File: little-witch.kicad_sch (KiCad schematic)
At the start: 30 parts, among them J1 GCT-USB4105, J3 Conn_ARM_SWD_TagConnect_TC203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, J4 GCT-USB4105, J5 Conn_02x20_Odd_Even, J6 BOOT0_SEL, SW1 SW_Push, U1 CH32V307RCT6, Y1 SIT8008BI-73-33N-25.000000

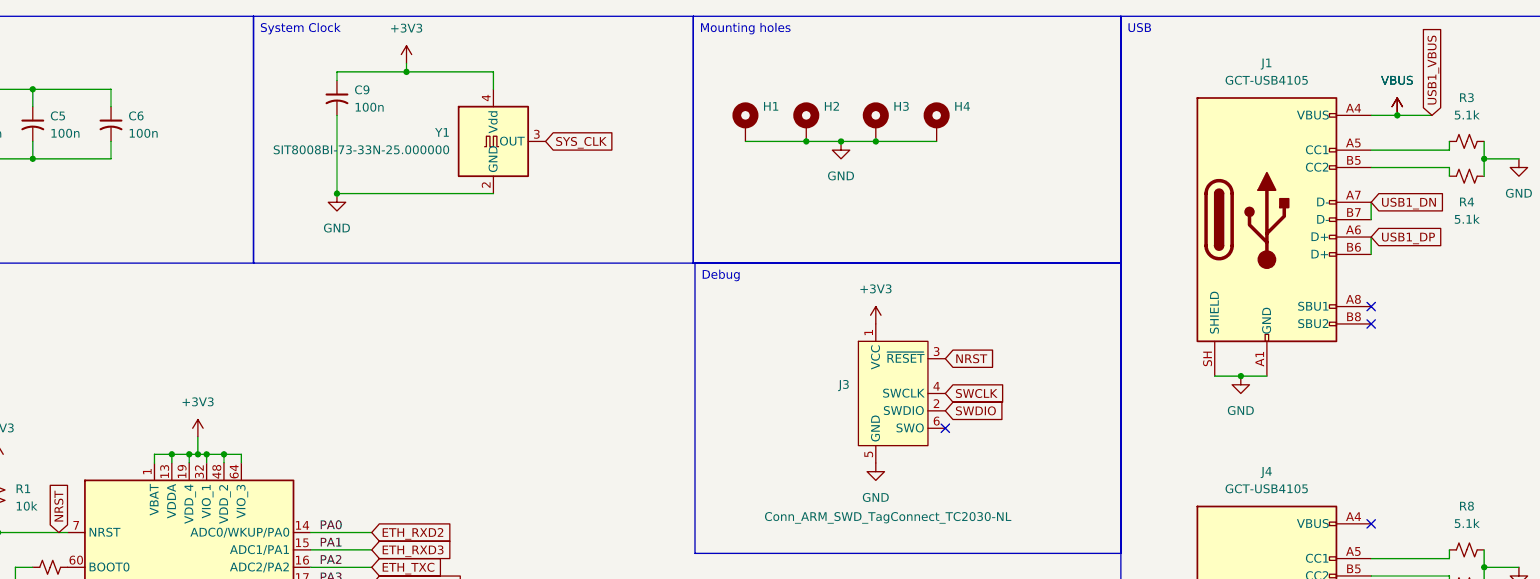
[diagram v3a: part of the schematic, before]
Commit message: Base ethernet signals routed
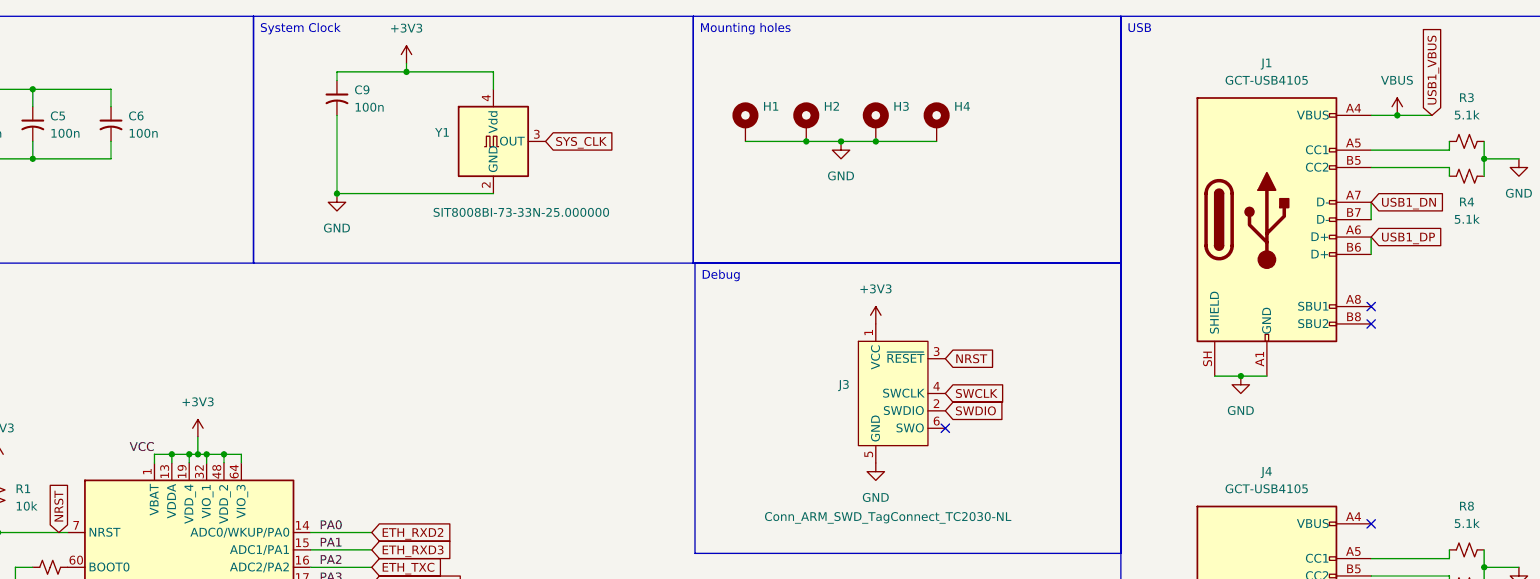
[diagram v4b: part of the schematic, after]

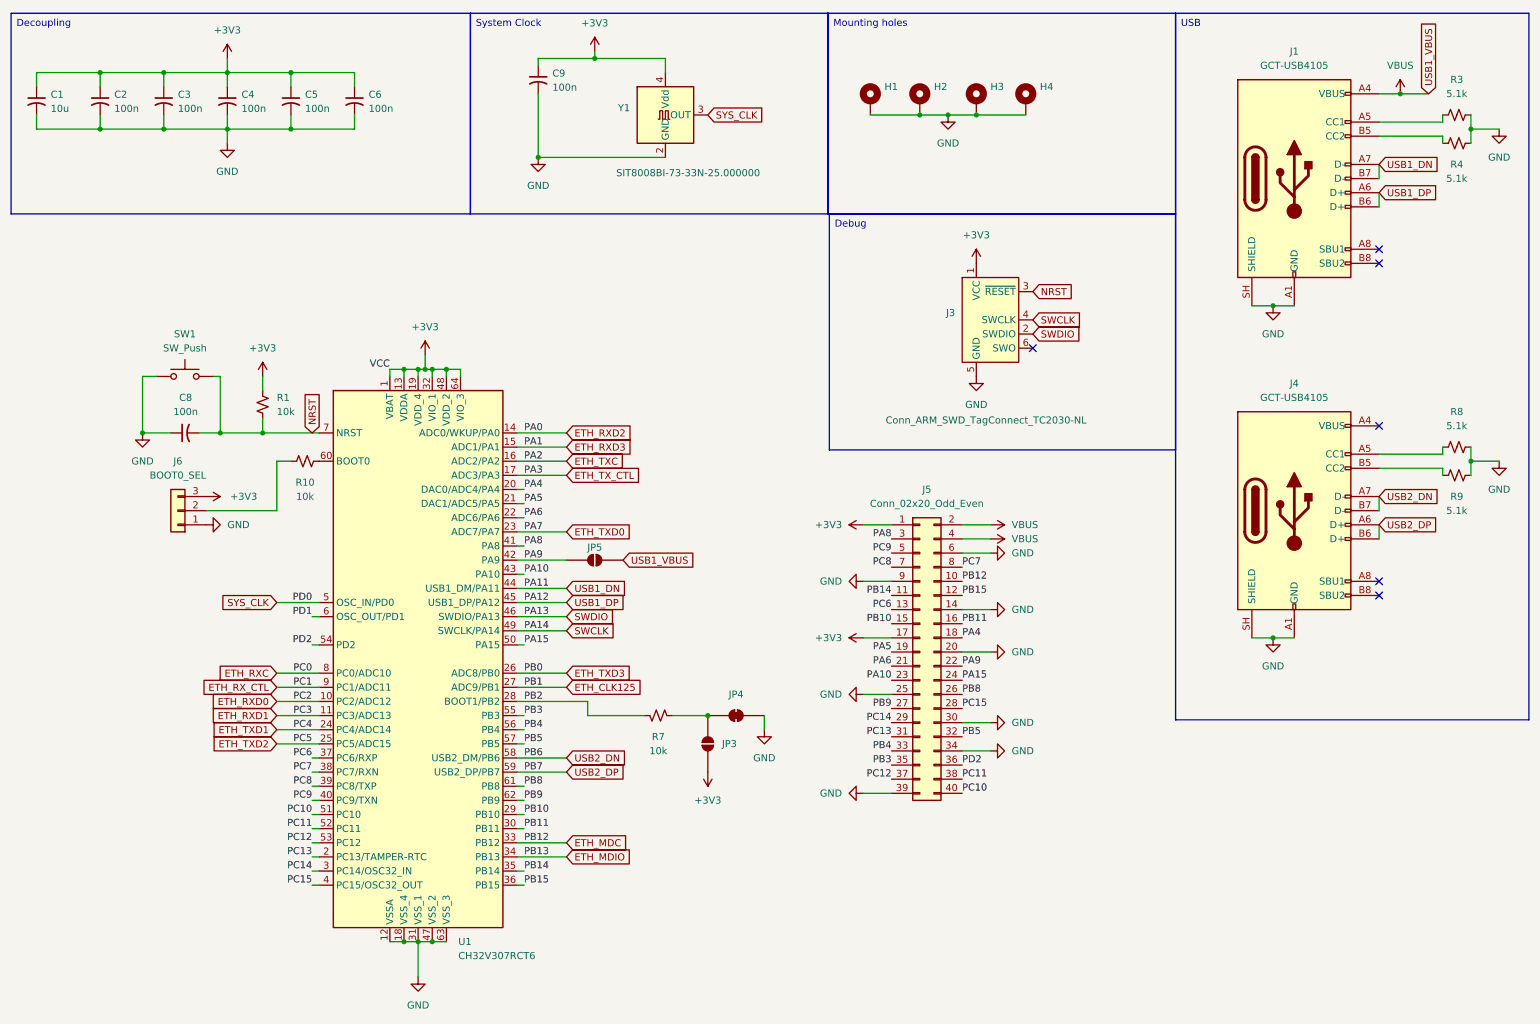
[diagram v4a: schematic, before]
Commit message: Some GPIO and power routing
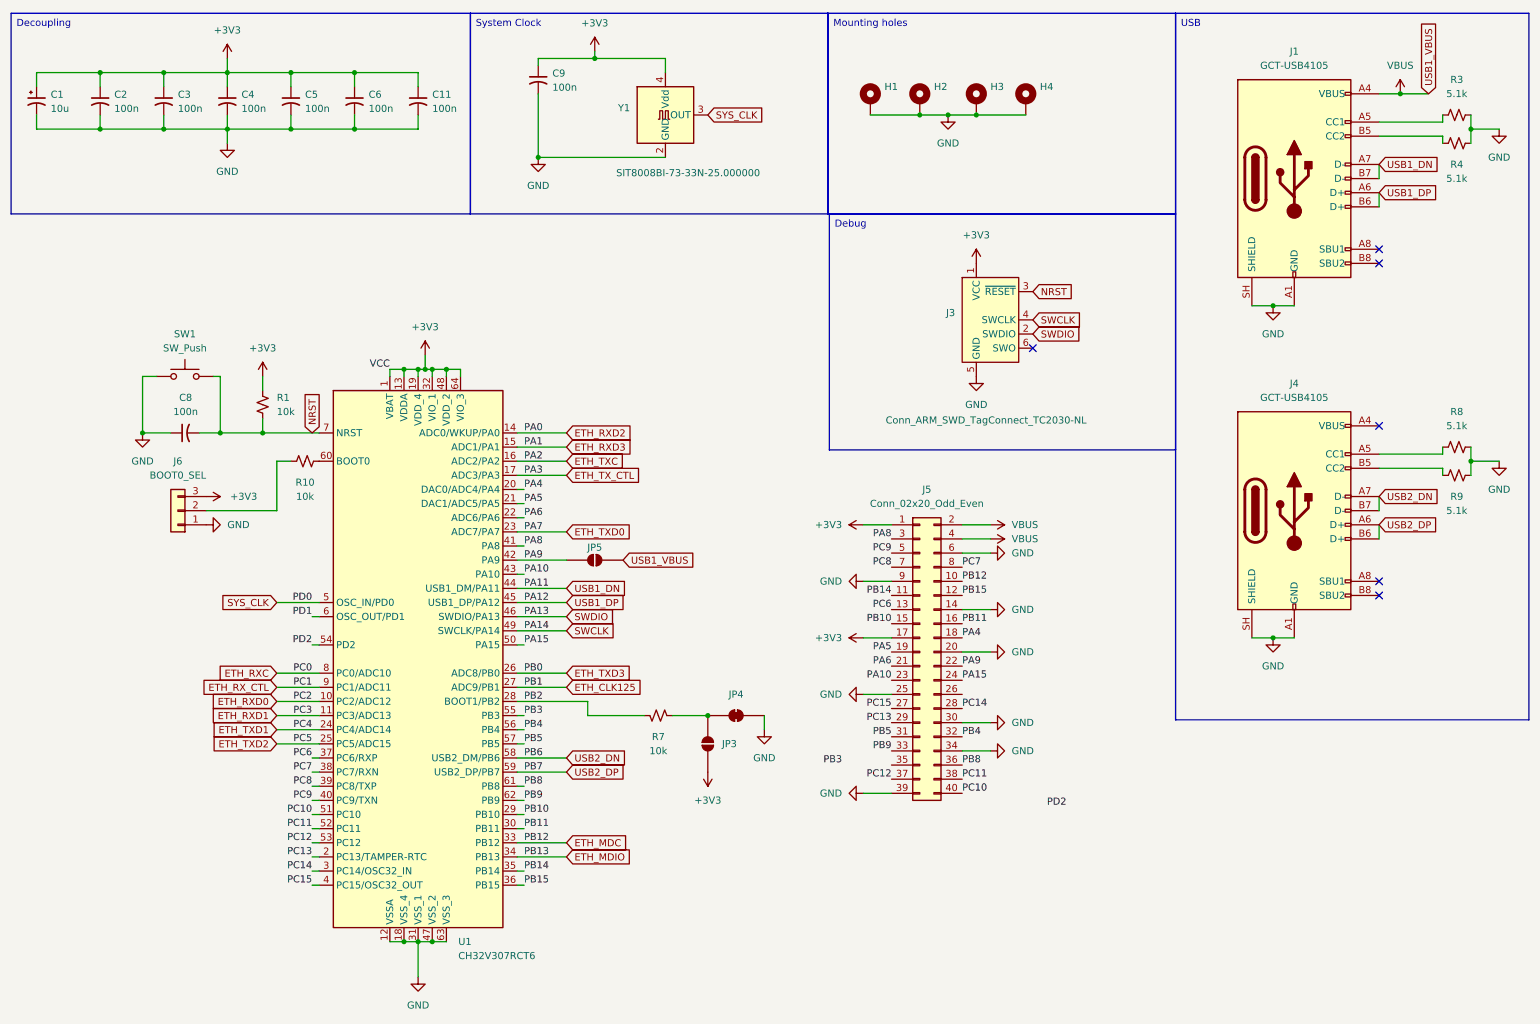
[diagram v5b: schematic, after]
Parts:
- added C11: 100n, Capacitor_SMD:C_0402_1005Metric, symbol Device:C_Small_US
- C1: footprint Capacitor_SMD:C_0402_1005Metric -> Capacitor_Tantalum_SMD:CP_EIA-2012-12_Kemet-R; symbol Device:C_Small_US -> Device:C_Polarized_Small_US
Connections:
- net +3V3: now also C11.1
- net GND: now also C11.2
- net PB3: no longer J5.35 (Pin_35)
- net PB4: now also J5.32 (Pin_32); no longer J5.33 (Pin_33)
- net PB5: now also J5.31 (Pin_31); no longer J5.32 (Pin_32)
- net PB8: now also J5.36 (Pin_36); no longer J5.26 (Pin_26)
- net PB9: now also J5.33 (Pin_33); no longer J5.27 (Pin_27)
- net PC13: now also J5.29 (Pin_29); no longer J5.31 (Pin_31)
- net PC14: now also J5.28 (Pin_28); no longer J5.29 (Pin_29)
- net PC15: now also J5.27 (Pin_27); no longer J5.28 (Pin_28)
- net PD2: no longer J5.36 (Pin_36)
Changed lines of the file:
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@@
 	)
 	(junction
+		(at 73.66 22.86)
+		(diameter 0)
+		(color 0 0 0 0)
+	)
+	(junction
 		(at 39.37 33.02)
 		(diameter 0)
@@
 	)
 	(junction
+		(at 73.66 33.02)
+		(diameter 0)
+		(color 0 0 0 0)
+	)
+	(junction
 		(at 87.63 76.2)
 		(diameter 0)
@@
 	(wire
 		(pts
+			(xy 85.09 33.02) (xy 85.09 30.48)
+		)
+		(stroke
+			(width 0)
+			(type default)
+		)
+	)
+	(wire
+		(pts
 			(xy 35.56 77.47) (xy 38.1 77.47)
 		)
@@
 	(wire
 		(pts
+			(xy 85.09 22.86) (xy 85.09 25.4)
+		)
+		(stroke
+			(width 0)
+			(type default)
+		)
+	)
+	(wire
+		(pts
 			(xy 87.63 76.2) (xy 90.17 76.2)
 		)
@@
 	(wire
 		(pts
+			(xy 73.66 33.02) (xy 85.09 33.02)
+		)
+		(stroke
+			(width 0)
+			(type default)
+		)
+	)
+	(wire
+		(pts
 			(xy 86.36 76.2) (xy 87.63 76.2)
 		)
@@
 	(wire
 		(pts
+			(xy 73.66 22.86) (xy 85.09 22.86)
+		)
+		(stroke
+			(width 0)
+			(type default)
+		)
+	)
+	(wire
+		(pts
 			(xy 116.84 20.32) (xy 129.54 20.32)
 		)
@@
 		)
 	)
-	(label "PC13"
-		(at 170.18 142.24 180)
-		(effects
-			(font
-				(size 1.27 1.27)
-			)
-			(justify right bottom)
-		)
-	)
 	(label "PC12"
 		(at 170.18 149.86 180)
@@
 		)
 	)
-	(label "PC14"
-		(at 170.18 139.7 180)
-		(effects
-			(font
-				(size 1.27 1.27)
-			)
-			(justify right bottom)
-		)
-	)
-	(label "PC15"
-		(at 182.88 137.16 0)
-		(effects
-			(font
-				(size 1.27 1.27)
-			)
-			(justify left bottom)
-		)
-	)
 	(label "PA13"
 		(at 104.14 120.65 0)
@@
 		)
 	)
-	(label "PB4"
-		(at 170.18 144.78 180)
-		(effects
-			(font
-				(size 1.27 1.27)
-			)
-			(justify right bottom)
-		)
-	)
 	(label "PB13"
 		(at 104.14 163.83 0)
@@
 		)
 	)
-	(label "PB5"
-		(at 182.88 142.24 0)
-		(effects
-			(font
-				(size 1.27 1.27)
-			)
-			(justify left bottom)
-		)
-	)
 	(label "PC6"
 		(at 66.04 146.05 180)
@@
 		)
 	)
+	(label "PC13"
+		(at 170.18 139.7 180)
+		(effects
+			(font
+				(size 1.27 1.27)
+			)
+			(justify right bottom)
+		)
+	)
 	(label "PB10"
 		(at 104.14 156.21 0)
@@
 		)
 	)
-	(label "PB8"
-		(at 182.88 134.62 0)
-		(effects
-			(font
-				(size 1.27 1.27)
-			)
-			(justify left bottom)
-		)
-	)
 	(label "PB3"
 		(at 104.14 138.43 0)
@@
 		)
 	)
+	(label "PB3"
+		(at 161.29 147.32 180)
+		(effects
+			(font
+				(size 1.27 1.27)
+			)
+			(justify right bottom)
+		)
+	)
 	(label "PC0"
 		(at 66.04 130.81 180)
@@
 		)
 	)
+	(label "PB5"
+		(at 170.18 142.24 180)
+		(effects
+			(font
+				(size 1.27 1.27)
+			)
+			(justify right bottom)
+		)
+	)
+	(label "PC15"
+		(at 170.18 137.16 180)
+		(effects
+			(font
+				(size 1.27 1.27)
+			)
+			(justify right bottom)
+		)
+	)
 	(label "PA0"
 		(at 104.14 87.63 0)
@@
 	)
 	(label "PB9"
-		(at 170.18 137.16 180)
+		(at 104.14 153.67 0)
 		(effects
 			(font
 				(size 1.27 1.27)
 			)
-			(justify right bottom)
+			(justify left bottom)
 		)
 	)
-	(label "PB9"
-		(at 104.14 153.67 0)
+	(label "PD2"
+		(at 198.12 154.94 0)
 		(effects
 			(font
@@
 		)
 	)
-	(label "PD2"
+	(label "PB8"
 		(at 182.88 147.32 0)
 		(effects
@@
 		)
 	)
+	(label "PB9"
+		(at 170.18 144.78 180)
+		(effects
+			(font
+				(size 1.27 1.27)
+			)
+			(justify right bottom)
+		)
+	)
 	(label "PA4"
 		(at 182.88 124.46 0)
@@
 		)
 	)
-	(label "PC13"
-		(at 66.04 163.83 180)
+	(label "PB4"
+		(at 182.88 142.24 0)
 		(effects
 			(font
 				(size 1.27 1.27)
 			)
-			(justify right bottom)
+			(justify left bottom)
 		)
 	)
-	(label "PB6"
-		(at 104.14 146.05 0)
+	(label "PC14"
+		(at 182.88 137.16 0)
 		(effects
 			(font
@@
 		)
 	)
-	(label "PB3"
-		(at 170.18 147.32 180)
+	(label "PC13"
+		(at 66.04 163.83 180)
 		(effects
 			(font
@@
 		)
 	)
+	(label "PB6"
+		(at 104.14 146.05 0)
+		(effects
+			(font
+				(size 1.27 1.27)
+			)
+			(justify left bottom)
+		)
+	)
 	(label "PC8"
 		(at 170.18 111.76 180)
@@
 	)
 	(symbol
-		(lib_id "Device:C_Small_US")
+		(lib_id "Device:C_Polarized_Small_US")
 		(at 16.51 27.94 0)
 		(unit 1)
@@
 			)
 		)
-		(property "Footprint" "Capacitor_SMD:C_0402_1005Metric"
+		(property "Footprint" "Capacitor_Tantalum_SMD:CP_EIA-2012-12_Kemet-R"
 			(at 16.51 27.94 0)
 			(hide yes)
@@
 			)
 		)
-		(property "Description" "capacitor, small US symbol"
+		(property "Description" "Polarized capacitor, small US symbol"
 			(at 16.51 27.94 0)
 			(hide yes)
@@
 					(unit 1)
 				)
+			)
+		)
+	)
+	(symbol
+		(lib_id "Device:C_Small_US")
+		(at 85.09 27.94 0)
+		(unit 1)
+		(body_style 1)
+		(exclude_from_sim no)
+		(in_bom yes)
+		(on_board yes)
+		(in_pos_files yes)
+		(dnp no)
+		(property "Reference" "C11"
+			(at 87.63 26.7969 0)
+			(show_name no)
+			(do_not_autoplace no)
+			(effects
+				(font
+					(size 1.27 1.27)
+				)
+				(justify left)
+			)
+		)
+		(property "Value" "100n"
+			(at 87.63 29.3369 0)
+			(show_name no)
+			(do_not_autoplace no)
+			(effects
+				(font
+					(size 1.27 1.27)
+				)
+				(justify left)
+			)
+		)
+		(property "Footprint" "Capacitor_SMD:C_0402_1005Metric"
+			(at 85.09 27.94 0)
+			(hide yes)
+			(show_name no)
+			(do_not_autoplace no)
+			(effects
+				(font
+					(size 1.27 1.27)
+				)
+			)
+		)
+		(property "Datasheet" ""
+			(at 85.09 27.94 0)
+			(hide yes)
+			(show_name no)
+			(do_not_autoplace no)
+			(effects
+				(font
+					(size 1.27 1.27)
+				)
+			)
+		)
+		(property "Description" "capacitor, small US symbol"
+			(at 85.09 27.94 0)
+			(hide yes)
+			(show_name no)
+			(do_not_autoplace no)
+			(effects
+				(font
+					(size 1.27 1.27)
+				)
+			)
+		)
+		(pin "2"
+		)
+		(pin "1"
+		)
+		(instances
+			(project "little-witch"
+				(path "/eaea4e42-a070-4be5-b9dd-9215ef3d72c7"
+					(reference "C11")
+					(unit 1)
+				)

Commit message: Continued GPIO
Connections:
- net ETH_CLK125 renamed PB1
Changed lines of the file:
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@@
-	(wire
-		(pts
-			(xy 102.87 133.35) (xy 111.76 133.35)
-		)
-		(stroke
-			(width 0)
-			(type default)
-		)
-	)
 	(wire
 		(pts
@@
 		(pts
 			(xy 27.94 22.86) (xy 27.94 25.4)
+		)
+		(stroke
+			(width 0)
+			(type default)
+		)
+	)
+	(wire
+		(pts
+			(xy 102.87 133.35) (xy 104.14 133.35)
 		)
 		(stroke
@@
 			)
 		)
-	)
-	(global_label "ETH_CLK125"
-		(shape input)
-		(at 111.76 133.35 0)
-		(fields_autoplaced yes)
-		(effects
-			(font
-				(size 1.27 1.27)
-			)
-			(justify left)
-		)
-		(property "Intersheetrefs" "${INTERSHEET_REFS}"
-			(at 126.3565 133.35 0)
-			(hide yes)
-			(show_name no)
-			(do_not_autoplace no)
-			(effects
-				(font
-					(size 1.27 1.27)
-				)
-				(justify left)
-			)
-		)

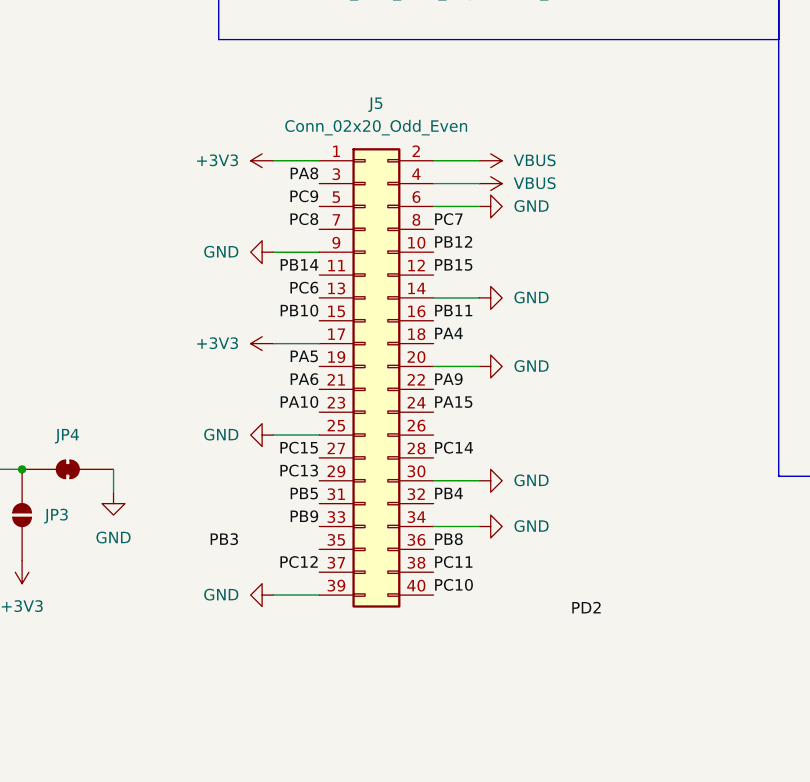
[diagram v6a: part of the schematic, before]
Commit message: GPIO routing
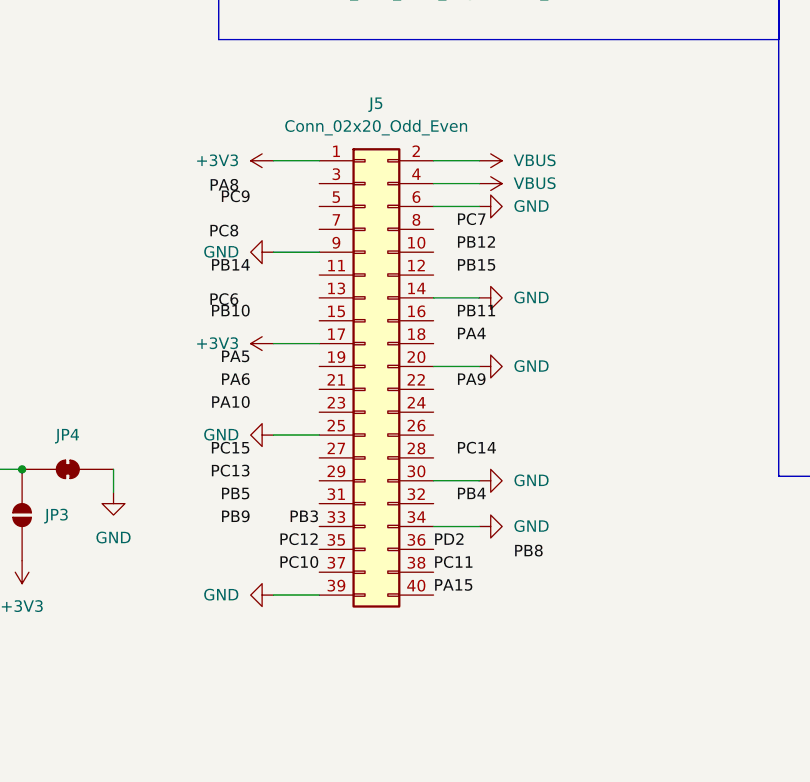
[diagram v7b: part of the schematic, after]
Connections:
- net ETH_MDC: no longer J5.10 (Pin_10)
- net PA10: no longer J5.23 (Pin_23)
- net PA15: now also J5.40 (Pin_40); no longer J5.24 (Pin_24)
- net PA4: no longer J5.18 (Pin_18)
- net PA5: no longer J5.19 (Pin_19)
- net PA6: no longer J5.21 (Pin_21)
- net PA8: no longer J5.3 (Pin_3)
- net PA9: no longer J5.22 (Pin_22)
- net PB10: no longer J5.15 (Pin_15)
- net PB11: no longer J5.16 (Pin_16)
- net PB14: no longer J5.11 (Pin_11)
- net PB15: no longer J5.12 (Pin_12)
- net PB3: now also J5.33 (Pin_33)
- net PB4: no longer J5.32 (Pin_32)
- net PB5: no longer J5.31 (Pin_31)
- net PB8: no longer J5.36 (Pin_36)
- net PB9: no longer J5.33 (Pin_33)
- net PC10: now also J5.37 (Pin_37); no longer J5.40 (Pin_40)
- net PC12: now also J5.35 (Pin_35); no longer J5.37 (Pin_37)
- net PC13: no longer J5.29 (Pin_29)
- net PC14: no longer J5.28 (Pin_28)
- net PC15: no longer J5.27 (Pin_27)
- net PC6: no longer J5.13 (Pin_13)
- net PC7: no longer J5.8 (Pin_8)
- net PC8: no longer J5.7 (Pin_7)
- net PC9: no longer J5.5 (Pin_5)
- net PD2: now also J5.36 (Pin_36)
